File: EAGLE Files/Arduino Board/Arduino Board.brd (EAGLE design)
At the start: 72.4 x 67.3 mm, 12 parts

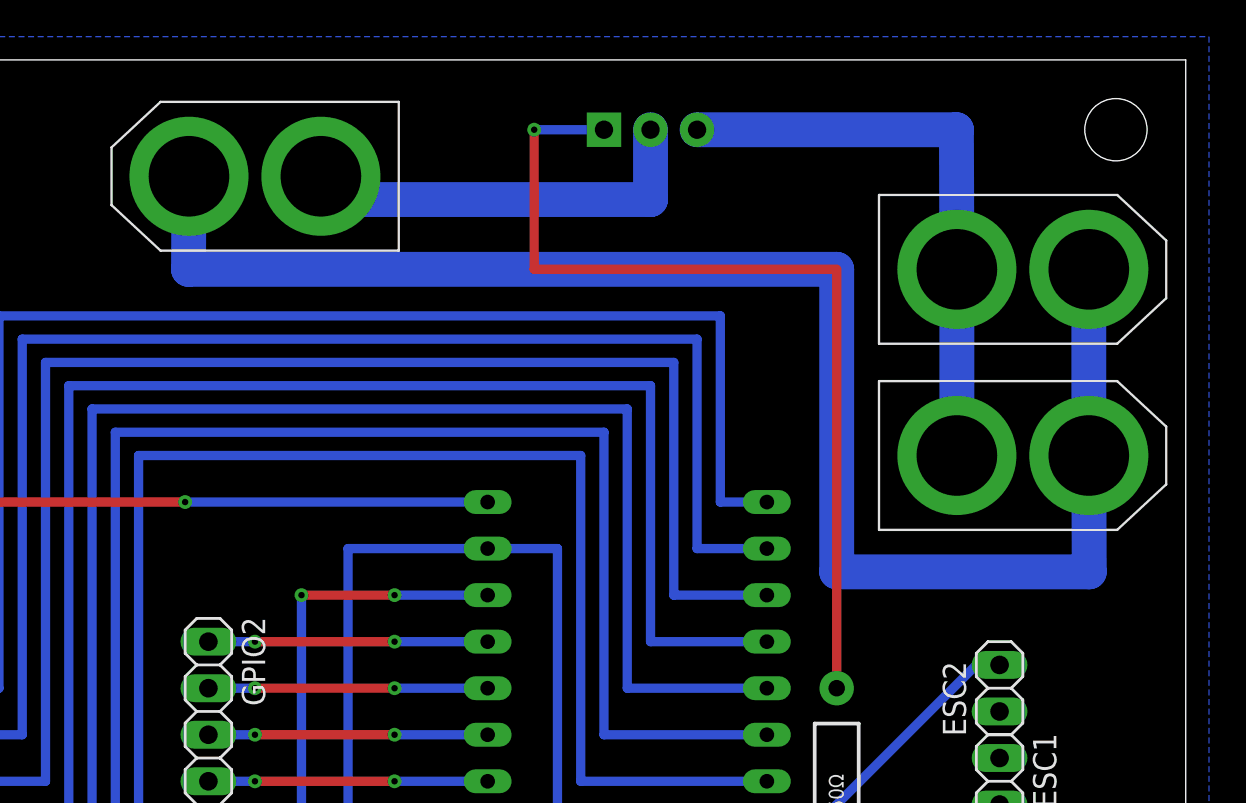
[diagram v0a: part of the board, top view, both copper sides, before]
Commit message: Corrected schematic error where MOSFET was wired incorrectly in circuit
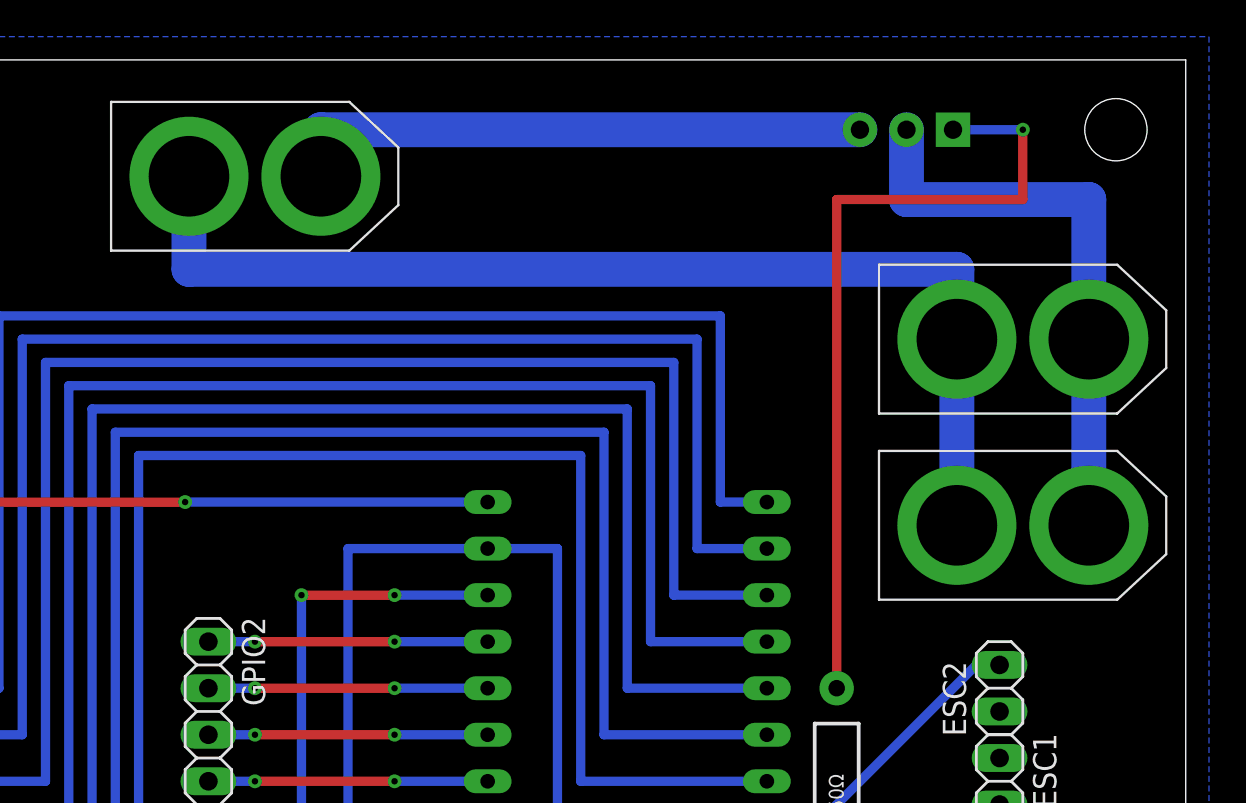
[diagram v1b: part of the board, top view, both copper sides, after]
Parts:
- moved POWER_MOSFET 14.0 mm to (57.1, 63.5), turned to 0 degrees
- moved ESC1_POWER 3.81 mm to (63.5, 41.9)
- moved ESC2_POWER 3.81 mm to (63.5, 52.1)
- turned BATTERY_POWER to 270 degrees
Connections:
- removed net REGULATED_SUPPLY+: ESC1_POWER.+, ESC2_POWER.+, POWER_MOSFET.3
- net GND: now also BATTERY_POWER.-, POWER_MOSFET.3
- net SUPPLY+: now also ESC1_POWER.+, ESC2_POWER.+; no longer POWER_MOSFET.2
- net SUPPLY-: now also POWER_MOSFET.2; no longer BATTERY_POWER.-
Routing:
- net SUPPLY-: track 87.3 -> 31.5 mm
- net SUPPLY+: track 23.0 -> 61.0 mm
- net GND: track 17.3 -> 49.2 mm
- net REGULATED_SUPPLY+: track 31.9 -> 0.00 mm
- net N$1: track 50.8 -> 44.4 mm
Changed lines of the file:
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@@
 </autorouter>
 <elements>
-<element name="BATTERY_POWER" library="Controls Library" package="XT60" value="XT60" x="21.59" y="60.96" rot="R90"/>
+<element name="BATTERY_POWER" library="Controls Library" package="XT60" value="XT60" x="21.59" y="60.96" rot="R270"/>
 <element name="ESC1" library="Controls Library" package="1X02" value="M02" x="62.23" y="27.94" rot="R270"/>
-<element name="ESC1_POWER" library="Controls Library" package="XT60" value="XT60" x="63.5" y="45.72" rot="R270"/>
+<element name="ESC1_POWER" library="Controls Library" package="XT60" value="XT60" x="63.5" y="41.91" rot="R270"/>
 <element name="ESC2" library="Controls Library" package="1X02" value="M02" x="62.23" y="33.02" rot="R90"/>
-<element name="ESC2_POWER" library="Controls Library" package="XT60" value="XT60" x="63.5" y="55.88" rot="R270"/>
+<element name="ESC2_POWER" library="Controls Library" package="XT60" value="XT60" x="63.5" y="52.07" rot="R270"/>
 <element name="GPIO1" library="Controls Library" package="1X08" value="" x="3.81" y="26.67" rot="R90"/>
 <element name="GPIO2" library="Controls Library" package="1X08" value="" x="19.05" y="26.67" rot="R270"/>
 <element name="IMU" library="Controls Library" package="1X08" value="" x="62.23" y="12.7" rot="R270"/>
 <element name="POWER" library="Controls Library" package="1X05" value="" x="24.13" y="7.62"/>
-<element name="POWER_MOSFET" library="Controls Library" package="TO-220-SINK" value="" x="43.18" y="63.5" rot="MR180">
-<attribute name="_EXTERNAL_" value="1" x="43.18" y="63.5" size="1.778" layer="28" rot="MR180" display="off"/>
+<element name="POWER_MOSFET" library="Controls Library" package="TO-220-SINK" value="" x="57.15" y="63.5" rot="MR0">
+<attribute name="_EXTERNAL_" value="1" x="57.15" y="63.5" size="1.778" layer="28" rot="MR0" display="off"/>
 </element>
 <element name="R1" library="Controls Library" package="AXIAL-0.4" value="250Ω" x="53.34" y="27.94" rot="R90"/>
@@
 <wire x1="19.939" y1="10.16" x2="19.05" y2="9.271" width="0.508" layer="16"/>
 <wire x1="19.05" y1="9.271" x2="19.05" y2="7.62" width="0.508" layer="16"/>
+<contactref element="POWER_MOSFET" pad="3"/>
+<contactref element="BATTERY_POWER" pad="-"/>
+<wire x1="25.19" y1="60.96" x2="25.19" y2="63.5" width="1.905" layer="16"/>
+<wire x1="25.19" y1="63.5" x2="54.61" y2="63.5" width="1.905" layer="16"/>
 </signal>
 <signal name="INT">
@@
 <signal name="SUPPLY+">
 <contactref element="BATTERY_POWER" pad="+"/>
-<contactref element="POWER_MOSFET" pad="2"/>
-<wire x1="43.18" y1="63.5" x2="43.18" y2="59.69" width="1.905" layer="16"/>
-<wire x1="25.215" y1="59.69" x2="25.19" y2="60.96" width="1.905" layer="16"/>
-<wire x1="43.18" y1="59.69" x2="25.215" y2="59.69" width="1.905" layer="16"/>
-</signal>
-<signal name="REGULATED_SUPPLY+">
-<contactref element="POWER_MOSFET" pad="3"/>
 <contactref element="ESC1_POWER" pad="+"/>
 <contactref element="ESC2_POWER" pad="+"/>
-<wire x1="59.9" y1="55.88" x2="59.9" y2="45.72" width="1.905" layer="16"/>
-<wire x1="45.72" y1="63.5" x2="59.875" y2="63.5" width="1.905" layer="16"/>
-<wire x1="59.875" y1="63.5" x2="59.9" y2="55.88" width="1.905" layer="16"/>
+<wire x1="59.9" y1="41.91" x2="59.9" y2="52.07" width="1.905" layer="16"/>
+<wire x1="59.9" y1="52.07" x2="59.9" y2="55.88" width="1.905" layer="16"/>
+<wire x1="59.9" y1="55.88" x2="17.99" y2="55.88" width="1.905" layer="16"/>
+<wire x1="17.99" y1="55.88" x2="17.99" y2="60.96" width="1.905" layer="16"/>
 </signal>
 <signal name="SUPPLY-">
 <contactref element="ESC1_POWER" pad="-"/>
-<contactref element="BATTERY_POWER" pad="-"/>
 <contactref element="ESC2_POWER" pad="-"/>
-<wire x1="67.1" y1="55.88" x2="67.1" y2="45.72" width="1.905" layer="16"/>
-<wire x1="67.1" y1="45.72" x2="67.125" y2="39.37" width="1.905" layer="16"/>
-<wire x1="53.34" y1="39.37" x2="67.125" y2="39.37" width="1.905" layer="16"/>
-<wire x1="17.99" y1="60.96" x2="17.965" y2="55.88" width="1.905" layer="16"/>
-<wire x1="53.34" y1="55.88" x2="53.34" y2="39.37" width="1.905" layer="16"/>
-<wire x1="17.965" y1="55.88" x2="53.34" y2="55.88" width="1.905" layer="16"/>
+<wire x1="67.1" y1="41.91" x2="67.1" y2="52.07" width="1.905" layer="16"/>
+<contactref element="POWER_MOSFET" pad="2"/>
+<wire x1="67.1" y1="59.69" x2="67.1" y2="52.07" width="1.905" layer="16"/>
+<wire x1="57.15" y1="63.5" x2="57.15" y2="59.69" width="1.905" layer="16"/>
+<wire x1="57.15" y1="59.69" x2="67.1" y2="59.69" width="1.905" layer="16"/>
 </signal>
 <signal name="N$1">
 <contactref element="R1" pad="P$2"/>
 <contactref element="POWER_MOSFET" pad="1"/>
-<wire x1="53.34" y1="33.02" x2="53.34" y2="55.88" width="0.508" layer="1"/>
-<wire x1="53.34" y1="55.88" x2="36.83" y2="55.88" width="0.508" layer="1"/>
-<wire x1="36.83" y1="55.88" x2="36.83" y2="63.5" width="0.508" layer="1"/>
-<via x="36.83" y="63.5" extent="1-16" drill="0.35"/>
-<wire x1="36.83" y1="63.5" x2="40.64" y2="63.5" width="0.508" layer="16"/>
+<wire x1="53.34" y1="33.02" x2="53.34" y2="59.69" width="0.508" layer="1"/>
+<wire x1="53.34" y1="59.69" x2="63.5" y2="59.69" width="0.508" layer="1"/>
+<wire x1="63.5" y1="59.69" x2="63.5" y2="63.5" width="0.508" layer="1"/>
+<via x="63.5" y="63.5" extent="1-16" drill="0.35"/>
+<wire x1="63.5" y1="63.5" x2="59.69" y2="63.5" width="0.508" layer="16"/>
 </signal>
 <signal name="D13">

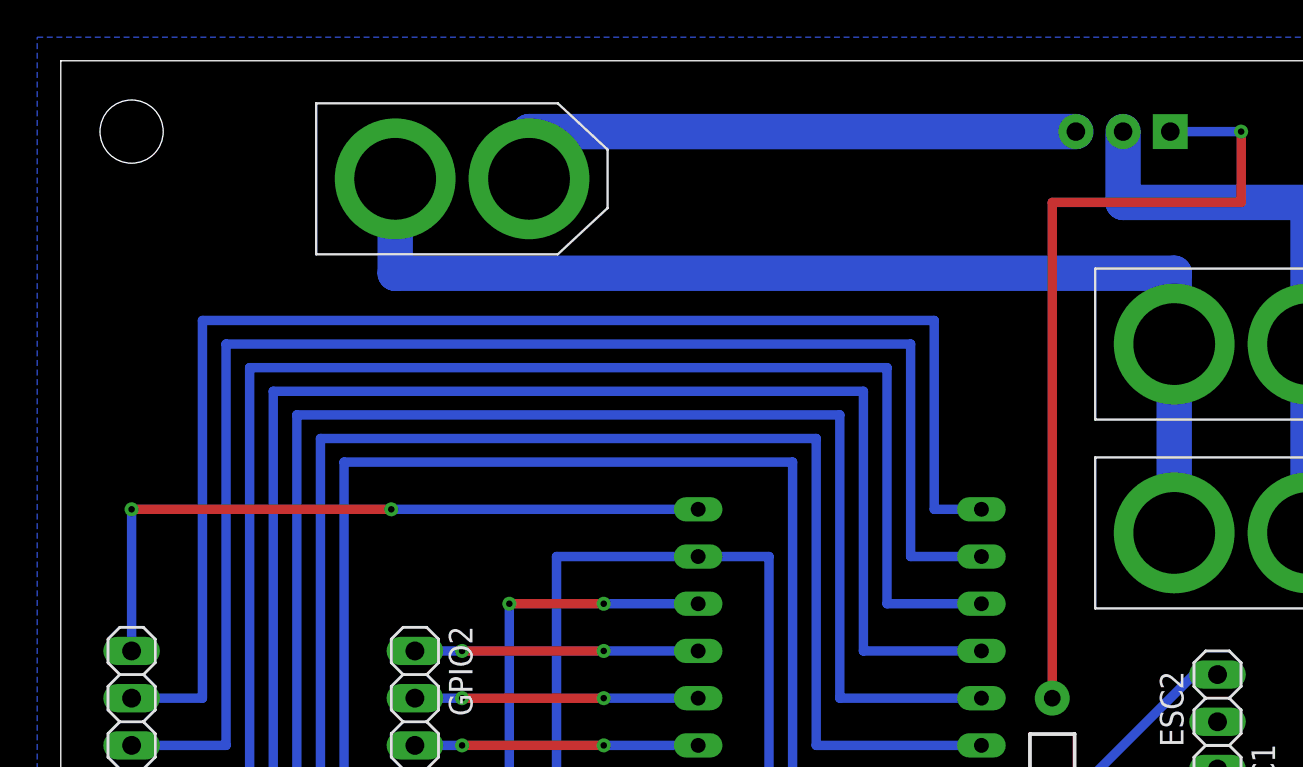
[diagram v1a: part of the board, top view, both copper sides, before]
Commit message: Added voltage divider for simple battery monitoring
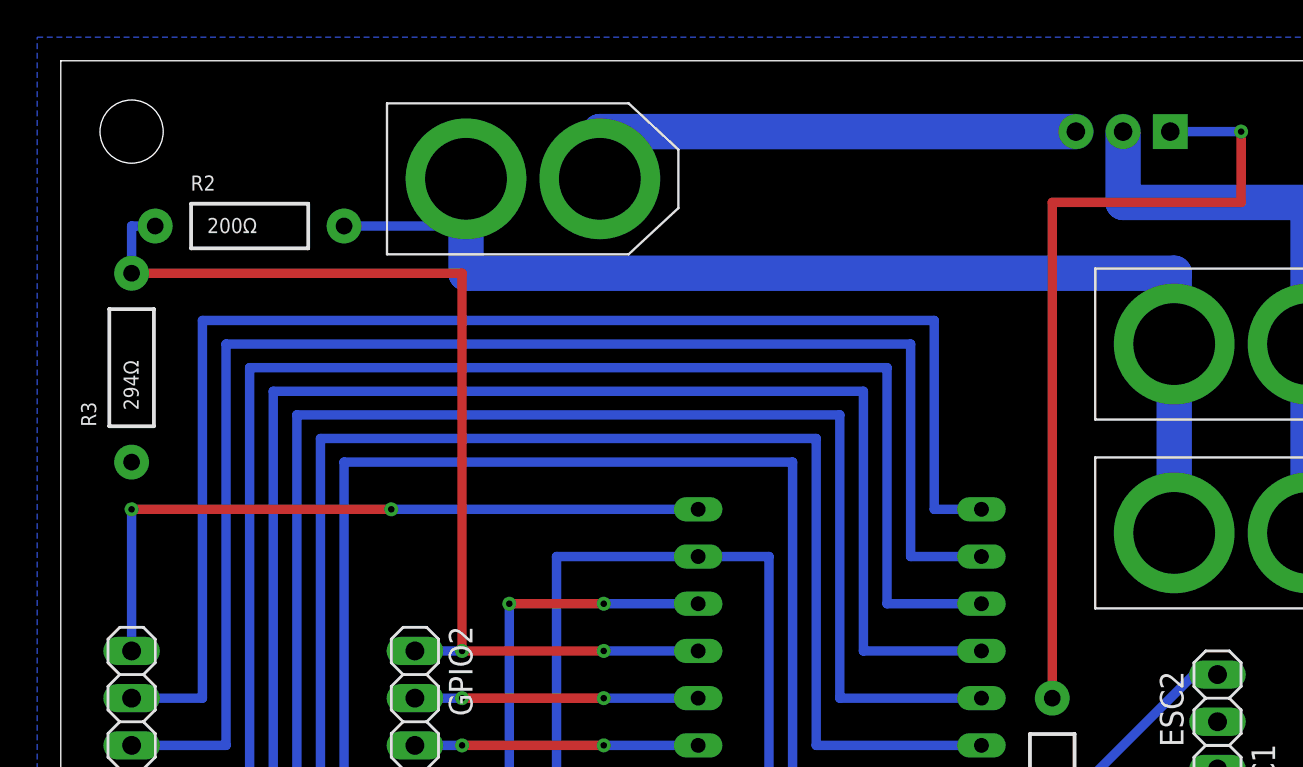
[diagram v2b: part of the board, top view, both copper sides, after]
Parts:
- added R2: 200Ω, Controls Library:AXIAL-0.4
- added R3: 294Ω, Controls Library:AXIAL-0.4
- moved BATTERY_POWER 3.81 mm to (25.4, 61.0)
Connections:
- net A0: now also R2.P$1, R3.P$2
- net GND: now also R3.P$1
- net SUPPLY+: now also R2.P$2
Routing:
- net A0: track 15.2 -> 57.1 mm
- net GND: track 49.2 -> 45.4 mm
- net SUPPLY+: track 61.0 -> 63.7 mm
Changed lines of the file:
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@@
 <?xml version="1.0" encoding="utf-8"?>
 <!DOCTYPE eagle SYSTEM "eagle.dtd">
-<eagle version="8.4.2">
+<eagle version="8.4.3">
 <drawing>
 <settings>
@@
 </autorouter>
 <elements>
-<element name="BATTERY_POWER" library="Controls Library" package="XT60" value="XT60" x="21.59" y="60.96" rot="R270"/>
+<element name="BATTERY_POWER" library="Controls Library" package="XT60" value="XT60" x="25.4" y="60.96" rot="R270"/>
 <element name="ESC1" library="Controls Library" package="1X02" value="M02" x="62.23" y="27.94" rot="R270"/>
 <element name="ESC1_POWER" library="Controls Library" package="XT60" value="XT60" x="63.5" y="41.91" rot="R270"/>
@@
 <element name="R1" library="Controls Library" package="AXIAL-0.4" value="250Ω" x="53.34" y="27.94" rot="R90"/>
 <element name="U$1" library="Controls Library" package="ARDUINO_NANO" value="ARDUINO_NANO" x="33.02" y="3.81"/>
+<element name="R2" library="Controls Library" package="AXIAL-0.4" value="200Ω" x="10.16" y="58.42"/>
+<element name="R3" library="Controls Library" package="AXIAL-0.4" value="294Ω" x="3.81" y="50.8" rot="R90"/>
 </elements>
 <signals>
@@
 <contactref element="POWER_MOSFET" pad="3"/>
 <contactref element="BATTERY_POWER" pad="-"/>
-<wire x1="25.19" y1="60.96" x2="25.19" y2="63.5" width="1.905" layer="16"/>
-<wire x1="25.19" y1="63.5" x2="54.61" y2="63.5" width="1.905" layer="16"/>
+<wire x1="29" y1="60.96" x2="29" y2="63.5" width="1.905" layer="16"/>
+<wire x1="29" y1="63.5" x2="54.61" y2="63.5" width="1.905" layer="16"/>
+<contactref element="R3" pad="P$1"/>
 </signal>
 <signal name="INT">
@@
 <wire x1="59.9" y1="41.91" x2="59.9" y2="52.07" width="1.905" layer="16"/>
 <wire x1="59.9" y1="52.07" x2="59.9" y2="55.88" width="1.905" layer="16"/>
-<wire x1="59.9" y1="55.88" x2="17.99" y2="55.88" width="1.905" layer="16"/>
-<wire x1="17.99" y1="55.88" x2="17.99" y2="60.96" width="1.905" layer="16"/>
+<wire x1="59.9" y1="55.88" x2="21.8" y2="55.88" width="1.905" layer="16"/>
+<wire x1="21.8" y1="58.42" x2="21.8" y2="55.88" width="1.905" layer="16"/>
+<contactref element="R2" pad="P$2"/>
+<wire x1="21.8" y1="58.42" x2="21.8" y2="60.96" width="1.905" layer="16"/>
+<wire x1="15.24" y1="58.42" x2="21.8" y2="58.42" width="0.508" layer="16"/>
 </signal>
 <signal name="SUPPLY-">
@@
 <wire x1="34.29" y1="35.56" x2="29.21" y2="35.56" width="0.508" layer="16"/>
 <via x="29.21" y="35.56" extent="1-16" drill="0.35"/>
-<wire x1="29.21" y1="35.56" x2="21.59" y2="35.56" width="0.508" layer="1"/>
+<wire x1="21.59" y1="35.56" x2="29.21" y2="35.56" width="0.508" layer="1"/>
 <via x="21.59" y="35.56" extent="1-16" drill="0.35"/>
 <wire x1="21.59" y1="35.56" x2="19.05" y2="35.56" width="0.508" layer="16"/>
+<contactref element="R2" pad="P$1"/>
+<contactref element="R3" pad="P$2"/>
+<wire x1="5.08" y1="58.42" x2="3.81" y2="58.42" width="0.508" layer="16"/>
+<wire x1="3.81" y1="58.42" x2="3.81" y2="55.88" width="0.508" layer="16"/>
+<wire x1="3.81" y1="55.88" x2="21.59" y2="55.88" width="0.508" layer="1"/>
+<wire x1="21.59" y1="55.88" x2="21.59" y2="35.56" width="0.508" layer="1"/>
 </signal>
 <signal name="A1">
